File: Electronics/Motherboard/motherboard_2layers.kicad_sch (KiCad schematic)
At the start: 54 parts, among them J2 Conn_02x10_Odd_Even, M1 AO3400A, M2 AO3400A, M3 AO3400A, U1 AMS1117-3.3, U6 LM2576HVS-5, U8 STM32F405RGTx

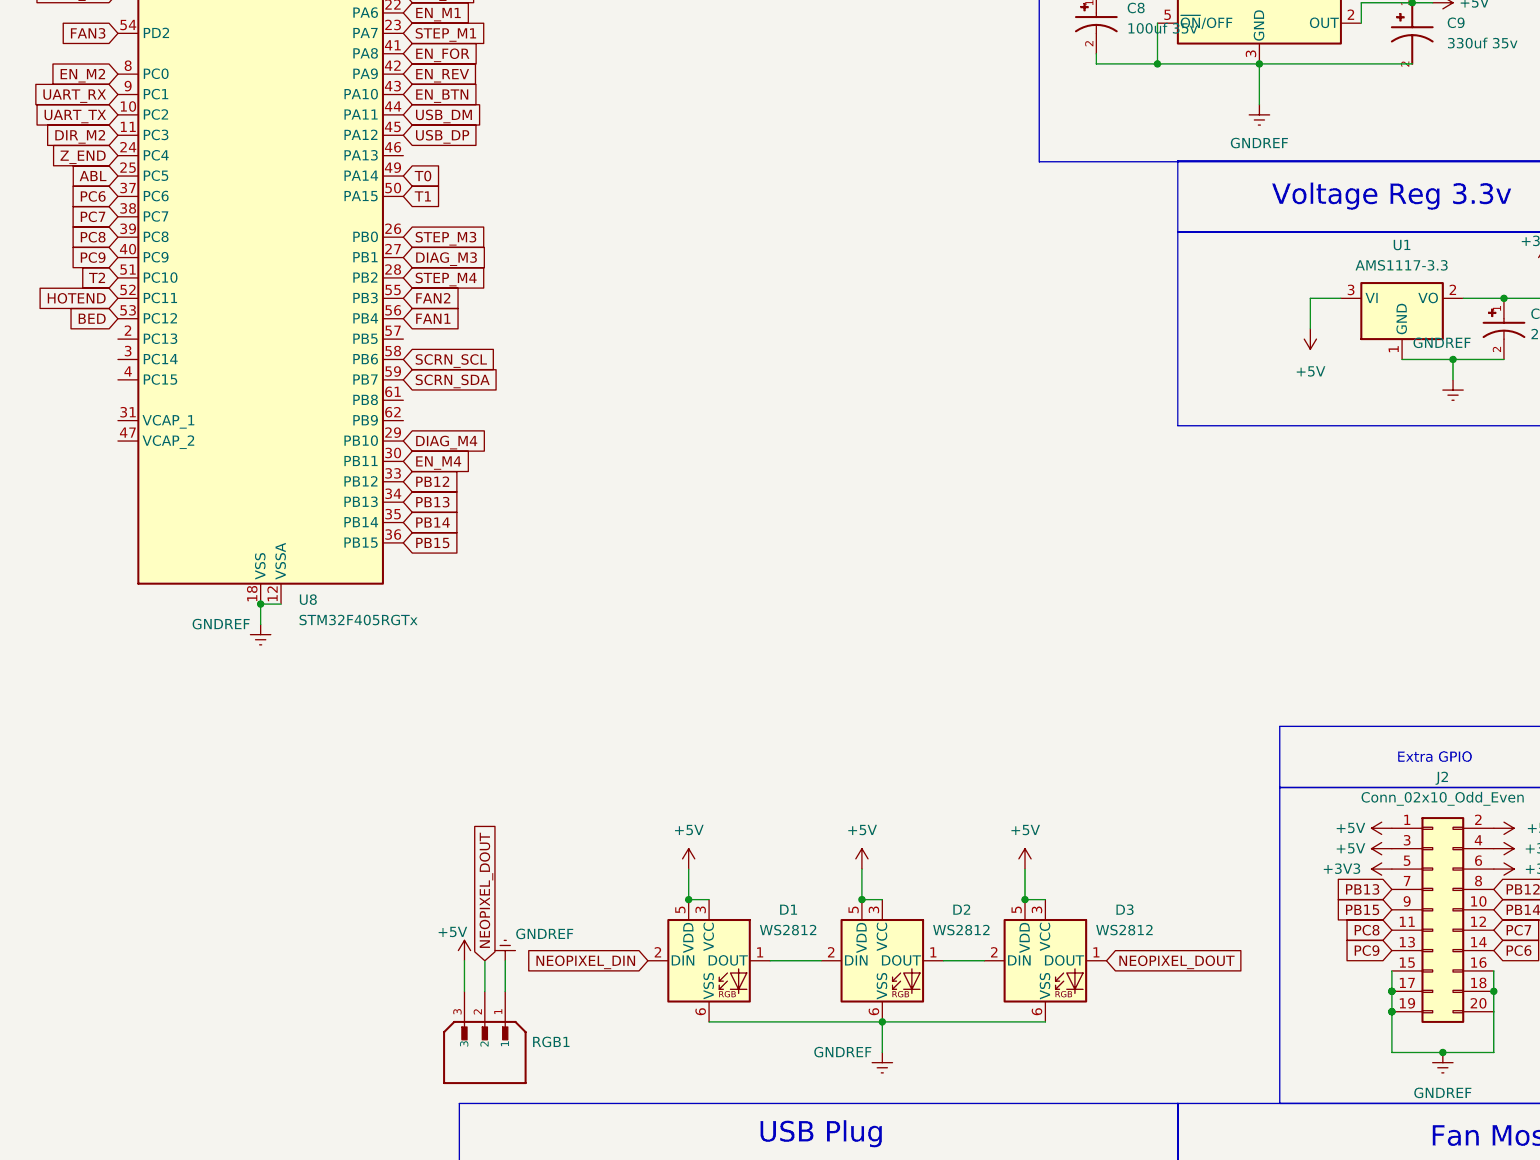
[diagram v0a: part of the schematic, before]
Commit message: Moved thermistor pins on the schematic around
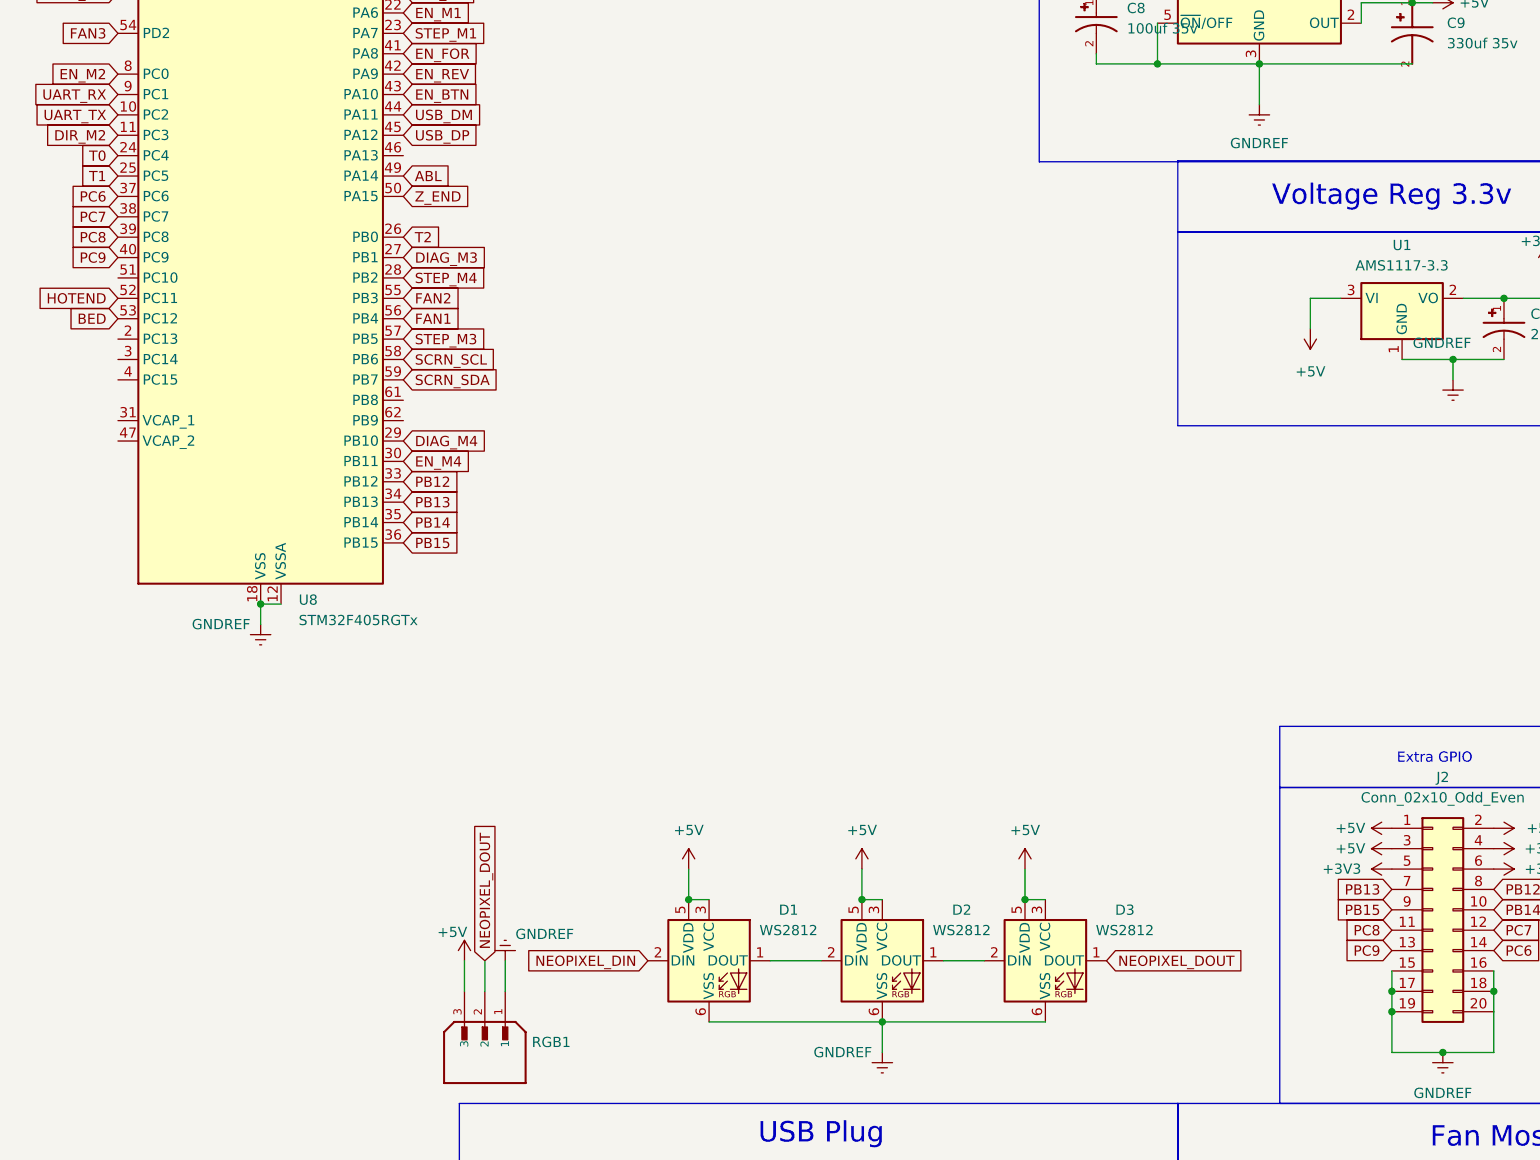
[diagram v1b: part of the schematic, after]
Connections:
- net ABL: now also U8.49 (PA14); no longer U8.25 (PC5)
- net STEP_M3: now also U8.57 (PB5); no longer U8.26 (PB0)
- net T0: now also U8.24 (PC4); no longer U8.49 (PA14)
- net T1: now also U8.25 (PC5); no longer U8.50 (PA15)
- net T2: now also U8.26 (PB0); no longer U8.51 (PC10)
- net Z_END: now also U8.50 (PA15); no longer U8.24 (PC4)
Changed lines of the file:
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@@
 	)
 	(junction
-		(at 203.2 218.44)
-		(diameter 0)
-		(color 0 0 0 0)
-	)
-	(junction
 		(at 284.48 34.29)
 		(diameter 0)
@@
 		(color 0 0 0 0)
 	)
-	(junction
-		(at 203.2 220.98)
-		(diameter 0)
-		(color 0 0 0 0)
-	)
 	(wire
 		(pts
@@
 		)
 	)
-	(global_label "ABL"
-		(shape input)
-		(at 44.45 116.84 180)
-		(fields_autoplaced yes)
-		(effects
-			(font
-				(size 1.27 1.27)
-			)
-			(justify right)
-		)
-		(property "Intersheetrefs" "${INTERSHEET_REFS}"
-			(at 38.0781 116.84 0)
-			(effects
-				(font
-					(size 1.27 1.27)
-				)
-				(justify right)
-				(hide yes)
-			)
-		)
-	)
 	(global_label "SCRN_SCL"
 		(shape input)
@@
 		)
 	)
+	(global_label "T2"
+		(shape input)
+		(at 80.01 124.46 0)
+		(fields_autoplaced yes)
+		(effects
+			(font
+				(size 1.27 1.27)
+			)
+			(justify left)
+		)
+		(property "Intersheetrefs" "${INTERSHEET_REFS}"
+			(at 85.1723 124.46 0)
+			(effects
+				(font
+					(size 1.27 1.27)
+				)
+				(justify left)
+				(hide yes)
+			)
+		)
+	)
 	(global_label "FAN3"
 		(shape input)
@@
 		)
 	)
+	(global_label "Z_END"
+		(shape input)
+		(at 80.01 119.38 0)
+		(fields_autoplaced yes)
+		(effects
+			(font
+				(size 1.27 1.27)
+			)
+			(justify left)
+		)
+		(property "Intersheetrefs" "${INTERSHEET_REFS}"
+			(at 88.9218 119.38 0)
+			(effects
+				(font
+					(size 1.27 1.27)
+				)
+				(justify left)
+				(hide yes)
+			)
+		)
+	)
 	(global_label "STEP_M4"
 		(shape input)
@@
 		)
 	)
-	(global_label "Z_END"
+	(global_label "T0"
 		(shape input)
-		(at 394.97 163.83 180)
+		(at 44.45 114.3 180)
 		(fields_autoplaced yes)
 		(effects
@@
 		)
 		(property "Intersheetrefs" "${INTERSHEET_REFS}"
-			(at 386.0582 163.83 0)
+			(at 39.2877 114.3 0)
 			(effects
 				(font
@@
 		)
 	)
-	(global_label "T0"
+	(global_label "Z_END"
 		(shape input)
-		(at 80.01 116.84 0)
+		(at 394.97 163.83 180)
 		(fields_autoplaced yes)
 		(effects
@@
 				(size 1.27 1.27)
 			)
-			(justify left)
+			(justify right)
 		)
 		(property "Intersheetrefs" "${INTERSHEET_REFS}"
-			(at 85.1723 116.84 0)
+			(at 386.0582 163.83 0)
 			(effects
 				(font
 					(size 1.27 1.27)
 				)
-				(justify left)
+				(justify right)
 				(hide yes)
 			)
@@
 		)
 	)
+	(global_label "ABL"
+		(shape input)
+		(at 80.01 116.84 0)
+		(fields_autoplaced yes)
+		(effects
+			(font
+				(size 1.27 1.27)
+			)
+			(justify left)
+		)
+		(property "Intersheetrefs" "${INTERSHEET_REFS}"
+			(at 86.3819 116.84 0)
+			(effects
+				(font
+					(size 1.27 1.27)
+				)
+				(justify left)
+				(hide yes)
+			)
+		)
+	)
 	(global_label "PB13"
 		(shape input)
@@
 		)
 	)
+	(global_label "T1"
+		(shape input)
+		(at 44.45 116.84 180)
+		(fields_autoplaced yes)
+		(effects
+			(font
+				(size 1.27 1.27)
+			)
+			(justify right)
+		)
+		(property "Intersheetrefs" "${INTERSHEET_REFS}"
+			(at 39.2877 116.84 0)
+			(effects
+				(font
+					(size 1.27 1.27)
+				)
+				(justify right)
+				(hide yes)
+			)
+		)
+	)
 	(global_label "EN_M2"
 		(shape input)
@@
 		)
 	)
-	(global_label "T2"
-		(shape input)
-		(at 44.45 129.54 180)
-		(fields_autoplaced yes)
-		(effects
-			(font
-				(size 1.27 1.27)
-			)
-			(justify right)
-		)
-		(property "Intersheetrefs" "${INTERSHEET_REFS}"
-			(at 39.2877 129.54 0)
-			(effects
-				(font
-					(size 1.27 1.27)
-				)
-				(justify right)
-				(hide yes)
-			)
-		)
-	)
-	(global_label "Z_END"
+	(global_label "STEP_M3"
 		(shape input)
-		(at 44.45 114.3 180)
+		(at 80.01 137.16 0)
 		(fields_autoplaced yes)
 		(effects
@@
 				(size 1.27 1.27)
 			)
-			(justify right)
+			(justify left)
 		)
 		(property "Intersheetrefs" "${INTERSHEET_REFS}"
-			(at 35.5382 114.3 0)
+			(at 91.2198 137.16 0)
 			(effects
 				(font
 					(size 1.27 1.27)
 				)
-				(justify right)
+				(justify left)
 				(hide yes)
 			)
@@
 		)
 	)
-	(global_label "STEP_M3"
-		(shape input)
-		(at 80.01 124.46 0)
-		(fields_autoplaced yes)
-		(effects
-			(font
-				(size 1.27 1.27)
-			)
-			(justify left)
-		)
-		(property "Intersheetrefs" "${INTERSHEET_REFS}"
-			(at 91.2198 124.46 0)
-			(effects
-				(font
-					(size 1.27 1.27)
-				)
-				(justify left)
-				(hide yes)
-			)
-		)
-	)
 	(global_label "NEOPIXEL_DIN"
 		(shape input)
@@
 				(hide yes)
 			)
-		)
-	)
-	(global_label "T1"
-		(shape input)
-		(at 80.01 119.38 0)
-		(fields_autoplaced yes)
-		(effects
-			(font
-				(size 1.27 1.27)
-			)
-			(justify left)
-		)
-		(property "Intersheetrefs" "${INTERSHEET_REFS}"
-			(at 85.1723 119.38 0)
-			(effects
-				(font
-					(size 1.27 1.27)
-				)
-				(justify left)
-				(hide yes)
-			)
